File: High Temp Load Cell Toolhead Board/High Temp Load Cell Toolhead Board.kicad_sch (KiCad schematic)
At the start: 100 parts, among them J1 Conn_01x03, J11 Conn_01x03, J12 Conn_01x03, J13 PinHeader_2x4_P2.54mm, J2 Conn_01x08, J3 Conn_01x04, J4 Conn_01x02, J5 Conn_01x02, J6 Conn_01x04, J7 Conn_01x02, J8 Conn_01x03, J9 Conn_01x02, Q1 DMG3404L, Q2 DMG3404L, SW1 SW_SPST, U1 MAX31865xTP, U2 STM32F103C8Tx, U3 74LVC1G17, U5 ADS1220xPW, X1 ECS-2520MV-080-CN-TR

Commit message: High Temp Toolhead Board
* Move different boards to directories
* check in the High Temp Tool Board work

delete autosaves
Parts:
- removed C30, C33: 0.1uF, Capacitor_SMD:C_0805_2012Metric, symbol Device:C
- removed D3, D4: LED, LED_SMD:LED_0603_1608Metric, symbol Device:LED
- removed J2: Conn_01x08, Molex CLIK-Mate:Molex_CLIK-Mate_502585-0870_1x08-1MP_P1.50mm_Horizontal, symbol Connector_Generic:Conn_01x08
- removed J3: Conn_01x04, Molex CLIK-Mate:Molex_CLIK-Mate_505405-0470_1x04-1MP_P1.50mm_Vertical, symbol Connector_Generic_MountingPin:Conn_01x04_MountingPin
- removed J4: Conn_01x02, Connector_Molex:Molex_Micro-Fit_3.0_43650-0215_1x02_P3.00mm_Vertical, symbol Connector_Generic_MountingPin:Conn_01x02_MountingPin
- removed J5: Conn_01x02, Connector_Molex:Molex_Micro-Fit_3.0_43650-0212_1x02-SMD_P3.00mm_Horizontal, symbol Connector_Generic_MountingPin:Conn_01x02_MountingPin
- removed R20, R28, R7: R10kΩ, Resistor_SMD:R_0603_1608Metric, symbol Device:R
- removed R24: R4.7kΩ, Resistor_SMD:R_0603_1608Metric, symbol Device:R
- removed R25: R10kΩ, Resistor_SMD:R_0603_1608Metric, symbol Device:R_Small
- removed R5, R6: 10K, Resistor_SMD:R_0603_1608Metric, symbol Device:R
- removed SW1: SW_SPST, Button_Switch_SMD:SW_Tactile_SPST_NO_Straight_CK_PTS636Sx25SMTRLFS, symbol KlipperExpander:SW_SPST
- removed VR1: TPSM861257RDXR, TPSM861_ultra:VREG_TPSM861253RDXR, symbol TPSM861_ultra:TPSM861253RDXR
- added C22, C23: 0.1uF, Capacitor_SMD:C_0603_1608Metric, symbol Device:C
- added D10, D9: AQ4020-01FTG-C, AQ4020-01FTG:SOD2613X114N, symbol AQ4020-01FTG:AQ4020-01FTG
- added D11, D7, D8: AQ4020-01FTG, AQ4020-01FTG:SOD2613X114N, symbol AQ4020-01FTG:AQ4020-01FTG
- added D12, D4: AQW05-01FTG, AQ4020-01FTG:SOD2613X114N, symbol AQ4020-01FTG:AQ4020-01FTG
- added D3: SMAJ24A, Diode_SMD:D_SMA, symbol Diode:SMAJ24CA
- added J2: Conn_02x08, Molex CLIK-Mate:Molex_CLIK-Mate_213226-0610_1x06-1MP_P1.50mm_Horizontal, symbol Connector_Generic_MountingPin:Conn_01x06_MountingPin
- added L10, L11, L12, L13, L6, L7, L8, L9: 120R@100MHz/3A, Inductor_SMD:L_0805_2012Metric, symbol Device:L_Ferrite
- added R13: R47Ω, Resistor_SMD:R_0603_1608Metric, symbol Device:R
- added R14: R1kΩ, Resistor_SMD:R_0603_1608Metric, symbol Device:R
- added SW1: SW_SPST, Button_Switch_SMD:SW_SPST_PTS810, symbol Switch:SW_SPST
- added U4: SN74AHC1G32QDBVRQ1, Package_TO_SOT_SMD:SOT-23-5, symbol 74xGxx:74AHC1G32
- added VR1: TLVM23615RDNR, SNAL_TLVM23615RDNR:CONV_TLVM23615RDNR, symbol TLVM23615RDNR:TLVM23615RDNR
- AC1: Manufacturer_Part_Number ADXL345 -> ADXL345TCCZ-EP-RL7; Part Number (none) -> ADXL345TCCZ-EP-RL7; Supplier (none) -> Digikey; Supplier_Link (none) -> https://www.digikey.com/en/products/detail/analog-devices-i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; Supplier_Part_Number (none) -> 505-ADXL345TCCZ-EP-RL7CT-ND
- C1: value 10uF -> 22uF
- C10: value 10nF -> 0.1uF
- C11, C12, C13, C14, C15, C16, C19, C20, C21, C25, C26, C27, C28, C29, C31, C32, C34, C36, C9: footprint Capacitor_SMD:C_0805_2012Metric -> Capacitor_SMD:C_0603_1608Metric
- C18: value 4.7uF -> 22uF
- C2: value 0.1uF -> 1uF
- C24: value 4.7uF -> 10uF
- C7: value 44uF -> 22uF
- C8: value 22pF -> 22uF; footprint Capacitor_SMD:C_0603_1608Metric -> Capacitor_SMD:C_1206_3216Metric
- D1: value SMAJ12A -> SMAJ24A; Manufacturer_Name (none) -> LITTELFUSE; Manufacturer_Part_Number (none) -> SMAJ6A; Part Number (none) -> LITTELFUSE; Supplier (none) -> Digikey; Supplier_Link (none) -> https://www.digikey.com/en/products/detail/littelfuse-inc/S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; Supplier_Part_Number (none) -> SMAJ6.0ALFCT-ND
- D2, D5, D6: value LED -> RED LED; Manufacturer_Name (none) -> Lite-On Inc.; Manufacturer_Part_Number (none) -> LTST-C193KRKT-5A; Part Number (none) -> LTST-C193KRKT-5A; Supplier (none) -> Digikey; Supplier_Link (none) -> https://www.digikey.com/en/products/detail/liteon/LTST-C193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; Supplier_Part_Number (none) -> 160-1830-1-ND
- J1: Manufacturer_Name (none) -> Molex; Manufacturer_Part_Number (none) -> 2132250370; Name (none) -> Hotend Fan; Supplier (none) -> Digikey; Supplier_Link (none) -> https://www.digikey.com/en/products/detail/molex/2132250370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; Supplier_Part_Number (none) -> 900-2132250370-ND
- J11: Manufacturer_Name (none) -> Molex; Manufacturer_Part_Number (none) -> 2132250370; Name (none) -> Print Fan; Supplier (none) -> Digikey; Supplier_Link (none) -> https://www.digikey.com/en/products/detail/molex/2132250370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; Supplier_Part_Number (none) -> 900-2132250370-ND
- J12: Manufacturer_Name (none) -> Molex; Manufacturer_Part_Number (none) -> 2132250370; Name (none) -> Filament Runout; Supplier (none) -> Digikey; Supplier_Link (none) -> https://www.digikey.com/en/products/detail/molex/2132250370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; Supplier_Part_Number (none) -> 900-2132250370-ND
- J13: footprint Connector_PinHeader_2.54mm:PinHeader_2x04_P2.54mm_Vertical -> Connector_PinHeader_2.54mm:PinHeader_2x03_P2.54mm_Vertical; symbol Connector_Generic:Conn_02x04_Odd_Even -> Connector_Generic:Conn_02x03_Odd_Even
- J6: Manufacturer_Name (none) -> Molex; Manufacturer_Part_Number (none) -> 2132250470; Name (none) -> Load Cell; Supplier (none) -> Digikey; Supplier_Link (none) -> https://www.digikey.com/en/products/detail/molex/2132250470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; Supplier_Part_Number (none) -> 900-2132250470-ND
- J7: Manufacturer_Name (none) -> Molex; Manufacturer_Part_Number (none) -> 2132250230; Name (none) -> PT100; Supplier (none) -> Digikey; Supplier_Link (none) -> https://www.digikey.com/en/products/detail/molex/2132250230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; Supplier_Part_Number (none) -> 900-2132250230CT-ND
- J8: value Conn_01x03 -> Conn_01x04; footprint Molex CLIK-Mate:Molex_CLIK-Mate_505405-0370_1x03-1MP_P1.50mm_Vertical -> Molex CLIK-Mate:Molex_CLIK-Mate_505405-0470_1x04-1MP_P1.50mm_Vertical; symbol Connector_Generic_MountingPin:Conn_01x03_MountingPin -> Connector_Generic_MountingPin:Conn_01x04_MountingPin; Manufacturer_Name (none) -> Molex; Manufacturer_Part_Number (none) -> 2132250370; Name (none) -> Neopixel; Supplier (none) -> Digikey; Supplier_Link (none) -> https://www.digikey.com/en/products/detail/molex/2132250370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; Supplier_Part_Number (none) -> 900-2132250370-ND
- J9: Manufacturer_Name (none) -> Molex; Manufacturer_Part_Number (none) -> 2132250230; Name (none) -> Heatbreak NTC; Supplier (none) -> Digikey; Supplier_Link (none) -> https://www.digikey.com/en/products/detail/molex/2132250230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; Supplier_Part_Number (none) -> 900-2132250230CT-ND
- LDO1: value LP5912-5.0DRV -> TPS7121-Q1 5V @ 500mA; footprint Package_SON:WSON-6-1EP_2x2mm_P0.65mm_EP1x1.6mm_ThermalVias -> Package_SON:VSON-8-1EP_3x3mm_P0.65mm_EP1.65x2.4mm_ThermalVias; symbol Regulator_Linear:LP5912-5.0DRV -> Project_Symbols:TPS7A21-Q1; Manufacturer_Name (none) -> Texas Instruments; Manufacturer_Part_Number (none) -> TPS7A2150PQWDRBRQ1; Supplier (none) -> Mouser; Supplier_Link (none) -> https://www.mouser.com/ProductDetail/Texas-Instruments/TPS7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; Supplier_Part_Number (none) -> 595-TPS7A2150PQWDRQ1
- LDO2: value LP5912-3.3DRV -> TPS7121-Q1 3.3V @ 500mA; footprint Package_SON:WSON-6-1EP_2x2mm_P0.65mm_EP1x1.6mm_ThermalVias -> Package_SON:VSON-8-1EP_3x3mm_P0.65mm_EP1.65x2.4mm_ThermalVias; symbol Regulator_Linear:LP5912-3.3DRV -> Project_Symbols:TPS7A21-Q1; Manufacturer_Name (none) -> Texas Instruments; Manufacturer_Part_Number (none) -> TPS7A2133PQWDRBRQ1; Supplier (none) -> Mouser; Supplier_Link (none) -> https://www.mouser.com/ProductDetail/Texas-Instruments/TPS7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; Supplier_Part_Number (none) -> 595-S7A2133PQWDRBRQ1
- Q1, Q2: Manufacturer_Name (none) -> Diodes Incorporated; Manufacturer_Part_Number (none) -> DMG3404L-7; Supplier (none) -> Digikey; Supplier_Link (none) -> https://www.digikey.com/en/products/detail/diodes-incorpora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; Supplier_Part_Number (none) -> DMG3404L-7DICT-ND
- R1: value R62kΩ -> R45.3kΩ
- R10: value R20Ω -> R1kΩ
- R11: value R20Ω -> R4.7kΩ
- R15: value R47Ω -> R1kΩ
- R19: value R10kΩ -> R1kΩ
- R2: value R30kΩ -> R10kΩ
- R26: value R4.7kΩ -> R1kΩ
- R28: renamed from R-Ref-PT1000; value R4300Ω 0.1% -> R430Ω; footprint Resistor_SMD:R_0805_2012Metric -> Resistor_SMD:R_0603_1608Metric
- R3: value R255kΩ -> R47Ω
- R4: value R30kΩ -> R1kΩ
- R9: value R10kΩ -> R2kΩ
- TH1: footprint Capacitor_SMD:C_0201_0603Metric -> Resistor_SMD:R_0603_1608Metric; Manufacturer_Name (none) -> Shenzhen Sunlord Electronics Co., Ltd.; Manufacturer_Part_Number (none) -> SDNT1608X104F3950FTF; Supplier (none) -> Digikey; Supplier_Link (none) -> https://www.digikey.com/en/products/detail/shenzhen-sunlord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; Supplier_Part_Number (none) -> 3442-SDNT1608X104F3950FTFCT-ND
- U1: Manufacturer_Name (none) -> MAX31865ATP+T; Manufacturer_Part_Number (none) -> MAX31865ATP+T; Supplier (none) -> Digikey; Supplier_Link (none) -> https://www.digikey.com/en/products/detail/analog-devices-i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; Supplier_Part_Number (none) -> MAX31865ATP+TCT-ND
- U2: value STM32F103C8Tx -> STM32F103CBU6TR; footprint Package_QFP:LQFP-48_7x7mm_P0.5mm -> Package_DFN_QFN:QFN-48-1EP_7x7mm_P0.5mm_EP5.6x5.6mm; symbol MCU_ST_STM32F1:STM32F103C8Tx -> MCU_ST_STM32F1:STM32F103CBUx; Manufacturer_Name (none) -> STMicroelectronics; Manufacturer_Part_Number (none) -> STM32F103CBU6TR; Supplier (none) -> Digikey; Supplier_Link (none) -> https://www.digikey.com/en/products/detail/stmicroelectroni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; Supplier_Part_Number (none) -> 497-18757-1-ND
- U3: value 74LVC1G17 -> SN74LVC2G17DSFR; footprint Level Shifter 74LVC1G17GV_125:SOT95P275X110-5N -> Package_TO_SOT_SMD:SOT-363_SC-70-6; symbol Project_Symbols:74LVC1G17GV,125 -> SN74LVC2G17DSFR:SN74LVC2G17DSFR; Supplier (none) -> Digikey; Supplier_Link (none) -> https://www.digikey.com/en/products/detail/nexperia-usa-inc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; Supplier_Part_Number (none) -> 1727-6070-1-ND
- U5: value ADS1220xPW -> ADS1220; footprint Package_SO:TSSOP-16_4.4x5mm_P0.65mm -> Package_DFN_QFN:Texas_RSA_VQFN-16-1EP_4x4mm_P0.65mm_EP2.7x2.7mm; Manufacturer_Name (none) -> Texas Instruments; Manufacturer_Part_Number (none) -> ADS1220IRVAR; Supplier (none) -> Digikey; Supplier_Link (none) -> https://www.digikey.com/en/products/detail/texas-instrument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; Supplier_Part_Number (none) -> 296-48475-1-ND
- X1: value ECS-2520MV-080-CN-TR -> ECS-2520MVLC-080-BP-TR; Manufacturer_Name (none) -> ECS Inc.; Manufacturer_Part_Number (none) -> ECS-2520MVLC-080-BP-TR; Supplier (none) -> Digikey; Supplier_Link (none) -> https://www.digikey.com/en/products/detail/ecs-inc/ECS-2520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; Supplier_Part_Number (none) -> 50-ECS-2520MVLC-080-BP-TRCT-ND
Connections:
- net +3V3: now also C20.2, R11.2, R15.1, R22.1, R23.2, R4.2, C22.2, C23.2, L7.1, R14.2, U4.3 (GND); no longer C27.2, C29.2, J12.1 (Pin_1), R21.2, R22.2, R23.1, R26.2
- net +5V: now also C17.1, C18.1, C29.1, L2.2, R9.2, U5.9 (REFP0), L8.1; no longer C18.2, J8.1 (Pin_1)
- net ADS1220_DRDY: now also U2.45 (PB8); no longer U2.30 (PA9)
- net ADXL345_CS: now also U2.11 (PA1); no longer U2.46 (PB9)
- net AMBIENT_THERMISTOR: now also C28.1, R23.1, U2.20 (PB2); no longer U2.11 (PA1)
- net BOOT0: now also J13.1 (Pin_1); no longer J13.3 (Pin_3)
- net Earth_Protective: now also D3.1 (A1), J2.MP (MountPin)
- net FAN0_PWM: now also R19.2, U2.18 (PB0); no longer Q1.1 (G), U2.40 (PB4)
- net FAN0_TACH: now also U2.17 (PA7), D7.1 (K), R14.1; no longer U2.3 (PC14)
- net FAN1_PWM: now also R26.2, U2.14 (PA4); no longer Q2.1 (G), U2.41 (PB5)
- net FAN1_TACH: now also R4.1, U2.13 (PA3), D8.1 (K); no longer U2.2 (PC13)
- net FILAMENT_SW: now also C19.1, J12.2 (Pin_2), R11.1, U2.38 (PA15), D11.1 (K); no longer C19.2, J12.3 (Pin_3), R26.1, U2.43 (PB7)
- net GND: now also C17.2, C18.2, C19.2, C20.1, C27.2, C29.2, C8.2, D2.1 (K), D5.1 (K), L3.2, LDO1.3 (GND), LDO1.4 (GND), LDO1.6 (GND), LDO1.9 (GND), LDO2.3 (GND), LDO2.4 (GND), LDO2.6 (GND), LDO2.9 (GND), U2.49 (VSS), U3.2 (GND), U5.8 (REFN0), C22.1, C23.1, D10.2 (A), D11.2 (A), D12.2 (A), D3.2 (A2), D4.2 (A), D7.2 (A), D8.2 (A), D9.2 (A), J2.4 (Pin_4), J2.5 (Pin_5), L11.2, L6.2, L9.2, SW1.2 (B), U4.5 (VCC), VR1.1 (PGOOD), VR1.10 (GND), VR1.11 (RT); no longer C18.1, C19.1, C20.2, C27.1, C29.1, J12.2 (Pin_2), J8.3 (Pin_3), J9.1 (Pin_1), LDO1.5 (GND), LDO2.5 (GND), R4.2, U3.3 (GND), U5.2 (~{CS})
- net HEATBREAK_THERMISTOR: now also C27.1, R22.2, U2.19 (PB1), L10.2; no longer C28.1, J9.2 (Pin_2), R22.1, U2.10 (PA0)
- net MAX31865_CS: now also U2.12 (PA2); no longer U2.21 (PB10)
- net NRST: now also SW1.1 (A); no longer J13.5 (Pin_5), R23.2
- net SPI_1_SCLK: now also U5.1 (SCLK), R13.2, U4.1; no longer U2.15 (PA5)
- net SPI_1_SDI: now also U2.40 (PB4), U5.15 (DOUT/~{DRDY}); no longer U2.16 (PA6)
- net SPI_1_SDO: now also U2.41 (PB5), U5.16 (DIN), U4.2; no longer AC1.13 (SDA/SDI/SDIO), U2.17 (PA7)
- net SPI_2_SCLK: now also R3.2, U3.3 (2A); no longer R15.1, U2.26 (PB13)
- net SPI_2_SDO: now also U3.1 (1A); no longer U5.16 (DIN)
- net SWD_IO: now also J13.5 (Pin_5); no longer J13.7 (Pin_7)
- net SW_CLK: now also J13.3 (Pin_3); no longer J13.8 (Pin_8)
- net USB_D+: now also R21.2, D9.1 (K), J2.1 (Pin_1); no longer R10.2, R21.1
- net USB_D-: now also D10.1 (K), J2.2 (Pin_2); no longer R11.2
- net USB_PULL_UP: now reaches U2.31 (PA10)
- net USB_PULL_UP: now also R10.2, R21.1
- net at U2.39 (PB3): now also R13.1
- net at L5.1: now also R16.2; no longer J6.2 (Pin_2)
- net LOAD_CELL_IN-: now reaches L5.2
- net LOAD_CELL_IN-: now also J6.3 (Pin_3); no longer R16.2
- net at D6.2 (A): now also R10.1
- net at D2.2 (A): now also R15.2; no longer R19.2
- net INPUT_24V+: now reaches D1.1 (A1), L1.1
- net INPUT_24V+: now also J2.6 (Pin_6)
- net LOAD_CELL_REF+: now reaches L2.1
- net LOAD_CELL_REF+: now also J6.1 (Pin_1); no longer J6.3 (Pin_3)
- net at R1.2, R2.1: now also VR1.9 (FB)
- net FAN0_MOSFET_GND: now reaches J1.1 (Pin_1), Q1.3 (D)
- net FAN0_MOSFET_GND: no longer D2.1 (K)
- net at C10.1, U1.5 (FORCE+), U1.7 (RTDIN+): now also L12.1; no longer J7.1 (Pin_1)
- net at C10.2, U1.8 (RTDIN-), U1.9 (FORCE-): now also L13.2; no longer J7.2 (Pin_2)
- net FAN1_MOSFET_GND: now reaches J11.1 (Pin_1), Q2.3 (D)
- net FAN1_MOSFET_GND: no longer D5.1 (K)
- net LED_CLK: now reaches U3.4 (2Y)
- net LED_CLK: now also J8.3 (Pin_3), D4.1 (K); no longer J8.2 (Pin_2)
- net at D5.2 (A): now also R9.1; no longer R9.2
- net LOAD_CELL_IN+: now reaches L4.1
- net LOAD_CELL_IN+: now also J6.2 (Pin_2); no longer J6.1 (Pin_1)
- net LOAD_CELL_REF-: now reaches J6.4 (Pin_4), L3.1
- removed net +12V: C1.1, C2.1, C20.1, J1.3 (Pin_3), J11.3 (Pin_3), L1.2, R1.1, R19.1, R9.1
- removed net +5V75: C4.1, C5.1, C7.1, C8.1, LDO1.4 (EN), LDO1.6 (IN), LDO2.4 (EN), LDO2.6 (IN), R3.1
- removed net BOOT1: J13.1 (Pin_1), U2.20 (PB2)
- removed net NEOPIXEL_DATA: U2.13 (PA3), U3.2 (A)
- net SPI_2_SDI: no longer names the net of U2.27 (PB14)
- net SPI_2_SDI: no longer U5.15 (DOUT/~{DRDY})
- new net: R3.1, U2.26 (PB13)
- new net: Q1.1 (G), R19.1
- new net: Q2.1 (G), R26.1
- new net: AC1.13 (SDA/SDI/SDIO), U4.4
- new net: C2.1, VR1.8 (VCC)
- new net +24V: C1.1, L1.2, VR1.2 (EN), VR1.3 (VIN)
- new net +5V5: C4.1, C5.1, C7.1, C8.1, LDO1.5 (EN), LDO1.8 (VIN), LDO2.5 (EN), LDO2.8 (VIN), R1.1, VR1.4 (VOUT)
- new net ADS1220_CS: U2.46 (PB9), U5.2 (~{CS})
- new net FILAMENT_SW_GND: J12.3 (Pin_3), L6.1
- new net FILAMENT_SW_V+: J12.1 (Pin_1), L7.2
- new net HEATBREAK_TH_GND: J9.2 (Pin_2), L11.1
- new net HEATBREAK_TH_VREF: J9.1 (Pin_1), L10.1
- new net INPUT_FANV+: J1.3 (Pin_3), J11.3 (Pin_3), J2.3 (Pin_3)
- new net LED_GND: J8.4 (Pin_4), L9.1
- new net LED_POWER: J8.1 (Pin_1), L8.2
- new net LED_SDI: D12.1 (K), J8.2 (Pin_2), U3.6 (1Y)
- new net PT100+: J7.2 (Pin_2), L12.2
- new net PT100-: J7.1 (Pin_1), L13.1
- no-connect marks 22 -> 26
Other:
- note added: "12V Power Input ESD and Conditioning"
- note added: "12V to 5.5V Switching Buck Converter Module"
- note added: "6V to 3.3V LDO"
- note added: "6V to 5V LDO"
- note added: "Ambient Thermistor"
- note added: "Connectors"
- note added: "Dotstar / Neopixel LED - with 3.3V to 5V 2-channel level shifter"
- note added: "Heatbreak Fan / Fan0"
- note added: "Heatbreak Thermistor"
- note added: "Indicator LEDs"
- note added: "MCU"
- note added: "Part Cooling Fan / Fan1"
- note added: "Reset Switch"
- note added: "Single Wire (SW) Debug Port"
- note added: "USB Data Line ESD and Full Speed Pull-Up"
- note removed: "12V Cooling Fans"
- note removed: "12V to 5.5V Switching Buck Converter"
- note removed: "24V Heater Passthrough"
- note removed: "5.5V to 3.3V LDO"
- note removed: "5.5V to 5V LDO"
- note removed: "Debug Port"
- note removed: "Input Connector"
- note removed: "Neopixel - 5V with 3.3V to 5V level shifter"
- note removed: "Power Conversion Block"
- note removed: "Stepper Passthrough"
- note removed: "Thermistors"
- moved on the sheet: AC1, C10, C11, C12, C13, C14, C15, C16, C17, C21, C24, C25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

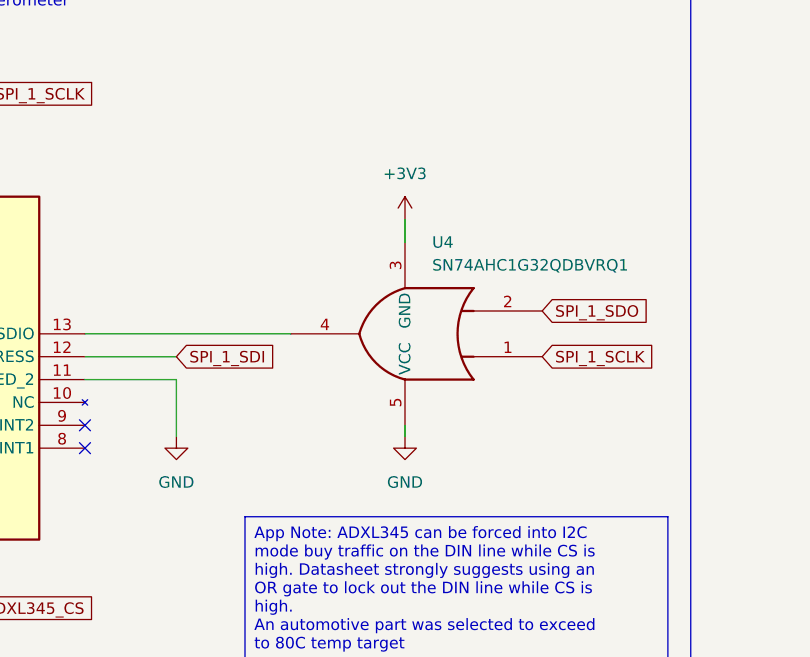
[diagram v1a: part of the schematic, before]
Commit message: Fix Incorrect Power Connections to ADXL or Gate
GND and VIN were reversed
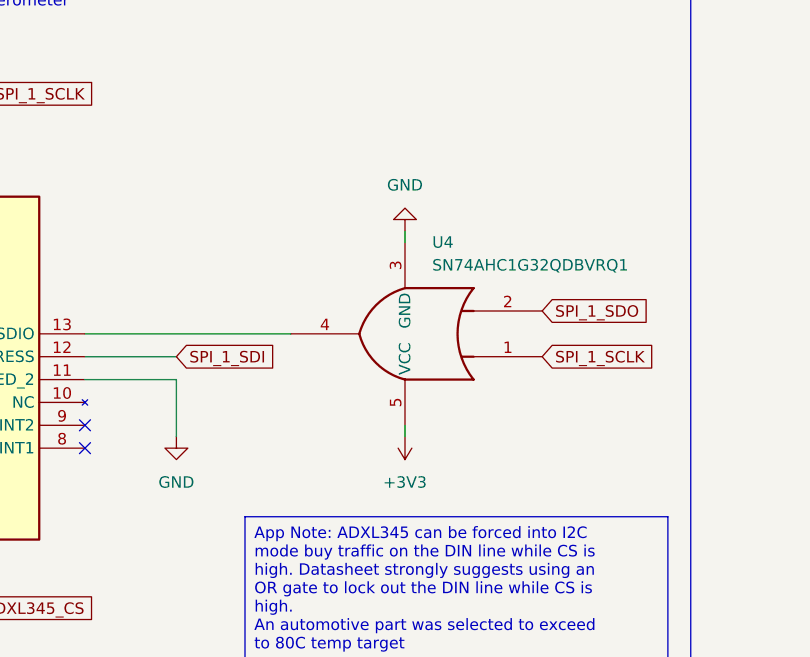
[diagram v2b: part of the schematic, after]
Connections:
- net +3V3: now also U4.5 (VCC); no longer U4.3 (GND)
- net GND: now also U4.3 (GND); no longer U4.5 (VCC)
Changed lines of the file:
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@@
 	(wire
 		(pts
-			(xy 510.54 207.01) (xy 510.54 209.55)
-		)
-		(stroke
-			(width 0)
-			(type default)
-		)
-	)
-	(wire
-		(pts
 			(xy 334.645 52.705) (xy 363.855 52.705)
 		)
@@
 	(wire
 		(pts
+			(xy 510.54 208.28) (xy 510.54 209.55)
+		)
+		(stroke
+			(width 0)
+			(type default)
+		)
+	)
+	(wire
+		(pts
 			(xy 307.34 174.625) (xy 323.85 174.625)
 		)
@@
 	(wire
 		(pts
+			(xy 510.54 231.14) (xy 510.54 229.87)
+		)
+		(stroke
+			(width 0)
+			(type default)
+		)
+	)
+	(wire
+		(pts
 			(xy 83.185 162.56) (xy 97.79 162.56)
 		)
@@
 	(wire
 		(pts
-			(xy 510.54 231.14) (xy 510.54 229.87)
-		)
-		(stroke
-			(width 0)
-			(type default)
-		)
-	)
-	(wire
-		(pts
 			(xy 156.21 218.44) (xy 147.32 218.44)
 		)
@@
 	)
 	(symbol
+		(lib_id "power:+3V3")
+		(at 510.54 231.14 180)
+		(unit 1)
+		(exclude_from_sim no)
+		(in_bom yes)
+		(on_board yes)
+		(dnp no)
+		(fields_autoplaced yes)
+		(property "Reference" "#PWR041"
+			(at 510.54 227.33 0)
+			(effects
+				(font
+					(size 1.27 1.27)
+				)
+				(hide yes)
+			)
+		)
+		(property "Value" "+3V3"
+			(at 510.54 236.22 0)
+			(effects
+				(font
+					(size 1.27 1.27)
+				)
+			)
+		)
+		(property "Footprint" ""
+			(at 510.54 231.14 0)
+			(effects
+				(font
+					(size 1.27 1.27)
+				)
+				(hide yes)
+			)
+		)
+		(property "Datasheet" ""
+			(at 510.54 231.14 0)
+			(effects
+				(font
+					(size 1.27 1.27)
+				)
+				(hide yes)
+			)
+		)
+		(property "Description" "Power symbol creates a global label with name \"+3V3\""
+			(at 510.54 231.14 0)
+			(effects
+				(font
+					(size 1.27 1.27)
+				)
+				(hide yes)
+			)
+		)
+		(pin "1"
+		)
+		(instances
+			(project "High Temp Load Cell Toolhead Board"
+				(path "/d7aad515-c17a-476a-b840-00742bfe5422"
+					(reference "#PWR041")
+					(unit 1)
+				)
+			)
+		)
+	)
+	(symbol
 		(lib_id "power:GND")
 		(at 52.705 110.49 0)
@@
 	)
 	(symbol
+		(lib_id "power:GND")
+		(at 510.54 208.28 0)
+		(mirror x)
+		(unit 1)
+		(exclude_from_sim no)
+		(in_bom yes)
+		(on_board yes)
+		(dnp no)
+		(fields_autoplaced yes)
+		(property "Reference" "#PWR058"
+			(at 510.54 201.93 0)
+			(effects
+				(font
+					(size 1.27 1.27)
+				)
+				(hide yes)
+			)
+		)
+		(property "Value" "GND"
+			(at 510.54 203.2 0)
+			(effects
+				(font
+					(size 1.27 1.27)
+				)
+			)
+		)
+		(property "Footprint" ""
+			(at 510.54 208.28 0)
+			(effects
+				(font
+					(size 1.27 1.27)
+				)
+				(hide yes)
+			)
+		)
+		(property "Datasheet" ""
+			(at 510.54 208.28 0)
+			(effects
+				(font
+					(size 1.27 1.27)
+				)
+				(hide yes)
+			)
+		)
+		(property "Description" "Power symbol creates a global label with name \"GND\" , ground"
+			(at 510.54 208.28 0)
+			(effects
+				(font
+					(size 1.27 1.27)
+				)
+				(hide yes)
+			)
+		)
+		(pin "1"
+		)
+		(instances
+			(project "High Temp Load Cell Toolhead Board"
+				(path "/d7aad515-c17a-476a-b840-00742bfe5422"
+					(reference "#PWR058")
+					(unit 1)
+				)
+			)
+		)
+	)
+	(symbol
 		(lib_id "Device:L_Ferrite")
 		(at 323.85 136.525 270)
@@
 	)
 	(symbol
-		(lib_id "power:+3V3")
-		(at 510.54 207.01 0)
-		(unit 1)
-		(exclude_from_sim no)
-		(in_bom yes)
-		(on_board yes)
-		(dnp no)
-		(fields_autoplaced yes)
-		(property "Reference" "#PWR041"
-			(at 510.54 210.82 0)
-			(effects
-				(font
-					(size 1.27 1.27)
-				)
-				(hide yes)
-			)
-		)
-		(property "Value" "+3V3"
-			(at 510.54 201.93 0)
-			(effects
-				(font
-					(size 1.27 1.27)
-				)
-			)
-		)
-		(property "Footprint" ""
-			(at 510.54 207.01 0)
-			(effects
-				(font
-					(size 1.27 1.27)
-				)
-				(hide yes)
-			)
-		)
-		(property "Datasheet" ""
-			(at 510.54 207.01 0)
-			(effects
-				(font
-					(size 1.27 1.27)
-				)
-				(hide yes)
-			)
-		)
-		(property "Description" "Power symbol creates a global label with name \"+3V3\""
-			(at 510.54 207.01 0)
-			(effects
-				(font
-					(size 1.27 1.27)
-				)
-				(hide yes)
-			)
-		)
-		(pin "1"
-		)
-		(instances
-			(project "High Temp Load Cell Toolhead Board"
-				(path "/d7aad515-c17a-476a-b840-00742bfe5422"
-					(reference "#PWR041")
-					(unit 1)
-				)
-			)
-		)
-	)
-	(symbol
 		(lib_id "power:+5V")
 		(at 427.99 118.11 0)
@@
 					(unit 1)
 				)
-			)
-		)
-	)
-	(symbol
-		(lib_id "power:GND")
-		(at 510.54 231.14 0)
-		(mirror y)
-		(unit 1)
-		(exclude_from_sim no)
-		(in_bom yes)
-		(on_board yes)
-		(dnp no)
-		(fields_autoplaced yes)
-		(property "Reference" "#PWR058"
-			(at 510.54 237.49 0)
-			(effects
-				(font
-					(size 1.27 1.27)
-				)
-				(hide yes)
-			)
-		)
-		(property "Value" "GND"
-			(at 510.54 236.22 0)
-			(effects
-				(font
-					(size 1.27 1.27)
-				)
-			)
-		)
-		(property "Footprint" ""
-			(at 510.54 231.14 0)
-			(effects
-				(font
-					(size 1.27 1.27)
-				)
-				(hide yes)
-			)
-		)
-		(property "Datasheet" ""
-			(at 510.54 231.14 0)
-			(effects
-				(font
-					(size 1.27 1.27)
-				)
-				(hide yes)
-			)
-		)
-		(property "Description" "Power symbol creates a global label with name \"GND\" , ground"
-			(at 510.54 231.14 0)
-			(effects
-				(font
-					(size 1.27 1.27)
-				)
-				(hide yes)
-			)
-		)
-		(pin "1"
-		)
-		(instances
-			(project "High Temp Load Cell Toolhead Board"
-				(path "/d7aad515-c17a-476a-b840-00742bfe5422"
-					(reference "#PWR058")
-					(unit 1)
-				)

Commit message: Re-work PCB for Grids
* Lay out components consistently using a 0.2mm grid
* Removes all grids that are not divisible by 0.1mm (gets rid of 'off by 0.05 errors')
* Brought back some more dense layouts with rows of components
* Reset all reference text positions so they align with components consistently
* References don't intersect with vias
* Improve how some traces enter/exit the chips using smaller vias and traces
* Removed resistor on the LED clock line as its not needed (klipper doesn't use real SPI for Dotstar)
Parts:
- removed R3: R47Ω, Resistor_SMD:R_0603_1608Metric, symbol Device:R
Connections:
- net ADXL345_CS: now also U4.1
- net SPI_1_SCLK: no longer U4.1
- net SPI_2_SCLK: now also U2.26 (PB13)
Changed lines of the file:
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@@
 	(wire
 		(pts
-			(xy 92.075 246.38) (xy 114.3 246.38)
-		)
-		(stroke
-			(width 0)
-			(type default)
-		)
-	)
-	(wire
-		(pts
 			(xy 109.22 92.71) (xy 109.22 97.79)
 		)
@@
 	(wire
 		(pts
-			(xy 80.645 246.38) (xy 84.455 246.38)
+			(xy 80.645 246.38) (xy 114.3 246.38)
 		)
 		(stroke
@@
 		)
 	)
-	(global_label "SPI_1_SCLK"
-		(shape input)
-		(at 525.78 222.25 0)
-		(fields_autoplaced yes)
-		(effects
-			(font
-				(size 1.27 1.27)
-			)
-			(justify left)
-		)
-		(property "Intersheetrefs" "${INTERSHEET_REFS}"
-			(at 539.7718 222.25 0)
-			(effects
-				(font
-					(size 1.27 1.27)
-				)
-				(justify left)
-				(hide yes)
-			)
-		)
-	)
 	(global_label "USB_PULL_UP"
 		(shape input)
@@
 		)
 	)
+	(global_label "ADXL345_CS"
+		(shape input)
+		(at 525.78 222.25 0)
+		(fields_autoplaced yes)
+		(effects
+			(font
+				(size 1.27 1.27)
+			)
+			(justify left)
+		)
+		(property "Intersheetrefs" "${INTERSHEET_REFS}"
+			(at 540.437 222.25 0)
+			(effects
+				(font
+					(size 1.27 1.27)
+				)
+				(justify left)
+				(hide yes)
+			)
+		)
+	)
 	(global_label "ADS1220_DRDY"
 		(shape input)
@@
 					(unit 1)
 				)
-			)
-		)
-	)
-	(symbol
-		(lib_id "Device:R")
-		(at 88.265 246.38 270)
-		(unit 1)
-		(exclude_from_sim no)
-		(in_bom yes)
-		(on_board yes)
-		(dnp no)
-		(fields_autoplaced yes)
-		(property "Reference" "R3"
-			(at 88.265 238.76 90)
-			(effects
-				(font
-					(size 1.27 1.27)
-				)
-			)
-		)
-		(property "Value" "R47Ω"
-			(at 88.265 241.3 90)
-			(effects
-				(font
-					(size 1.27 1.27)
-				)
-			)
-		)
-		(property "Footprint" "Resistor_SMD:R_0603_1608Metric"
-			(at 88.265 244.602 90)
-			(effects
-				(font
-					(size 1.27 1.27)
-				)
-				(hide yes)
-			)
-		)
-		(property "Datasheet" "~"
-			(at 88.265 246.38 0)
-			(effects
-				(font
-					(size 1.27 1.27)
-				)
-				(hide yes)
-			)
-		)
-		(property "Description" "50mW / 1%"
-			(at 88.265 243.84 90)
-			(effects
-				(font
-					(size 0.635 0.635)
-				)
-			)
-		)
-		(property "Supplier" ""
-			(at 88.265 246.38 0)
-			(effects
-				(font
-					(size 1.27 1.27)
-				)
-				(hide yes)
-			)
-		)
-		(property "Supplier_Link" ""
-			(at 88.265 246.38 0)
-			(effects
-				(font
-					(size 1.27 1.27)
-				)
-				(hide yes)
-			)
-		)
-		(property "Supplier_Part_Number" ""
-			(at 88.265 246.38 0)
-			(effects
-				(font
-					(size 1.27 1.27)
-				)
-				(hide yes)
-			)
-		)
-		(property "MAXIMUM_PACKAGE_HEIGHT" ""
-			(at 88.265 246.38 0)
-			(effects
-				(font
-					(size 1.27 1.27)
-				)
-				(hide yes)
-			)
-		)
-		(property "PARTREV" ""
-			(at 88.265 246.38 0)
-			(effects
-				(font
-					(size 1.27 1.27)
-				)
-				(hide yes)
-			)
-		)
-		(property "STANDARD" ""
-			(at 88.265 246.38 0)
-			(effects
-				(font
-					(size 1.27 1.27)
-				)
-				(hide yes)
-			)
-		)
-		(pin "2"
-		)
-		(pin "1"
-		)
-		(instances
-			(project "High Temp Load Cell Toolhead Board"
-				(path "/d7aad515-c17a-476a-b840-00742bfe5422"
-					(reference "R3")
-					(unit 1)
-				)

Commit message: Add Fan LEDs
* Add LEDs for both fans
* Reposition Earth to GND Diode to bottom of board for more LED space
* Re-run the via stitching, this time assuming tented vias can have solder mask on them
* Solved a problem with zone clearances, set all zone clearances to 0
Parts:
- added D13, D14: RED LED, LED_SMD:LED_0603_1608Metric, symbol Device:LED
- added R3, R5: R2kΩ, Resistor_SMD:R_0603_1608Metric, symbol Device:R
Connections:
- net FAN0_MOSFET_GND: now also D13.1 (K)
- net FAN1_MOSFET_GND: now also D14.1 (K)
- net INPUT_FANV+: now also R3.2, R5.2
- net SW_HEATSINK: now reaches VR1.5 (SW)
- new net: D14.2 (A), R5.1
- new net: D13.2 (A), R3.1
- no-connect marks 26 -> 25
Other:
- moved on the sheet: D2, D5, D6, R10, R15, R9

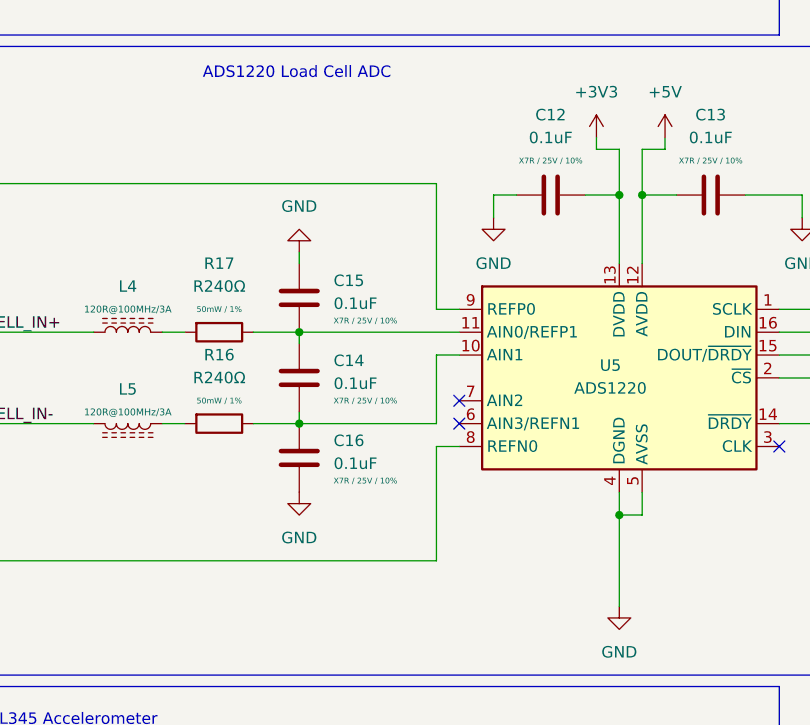
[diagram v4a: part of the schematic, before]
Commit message: Minor Updates
* Tweak ground plane min connection size to 0.2mm to improve the areas it can reach
* Updates to the ADS1220 layout
* Updates to the decoupling capacitors around the MCU
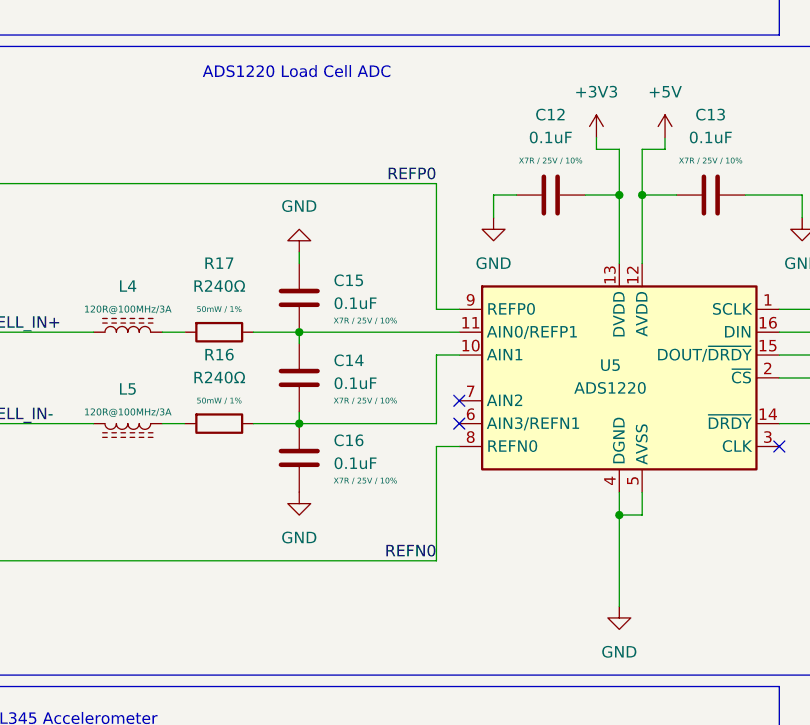
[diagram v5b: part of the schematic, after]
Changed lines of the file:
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@@
+		)
+	)
+	(label "REFN0"
+		(at 504.19 165.1 180)
+		(fields_autoplaced yes)
+		(effects
+			(font
+				(size 1.27 1.27)
+			)
+			(justify right bottom)
 		)
 	)
@@
 		)
 	)
+	(label "REFP0"
+		(at 504.19 123.19 180)
+		(fields_autoplaced yes)
+		(effects
+			(font
+				(size 1.27 1.27)
+			)
+			(justify right bottom)
+		)
+	)
